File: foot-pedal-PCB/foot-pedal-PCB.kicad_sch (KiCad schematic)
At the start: 14 parts, among them J1 Conn_01x01_Pin, J2 Conn_01x01_Pin, J3 Conn_01x01_Pin, J4 Conn_01x01_Pin, Q1 BT136-600E, SW1 CS12ANW03

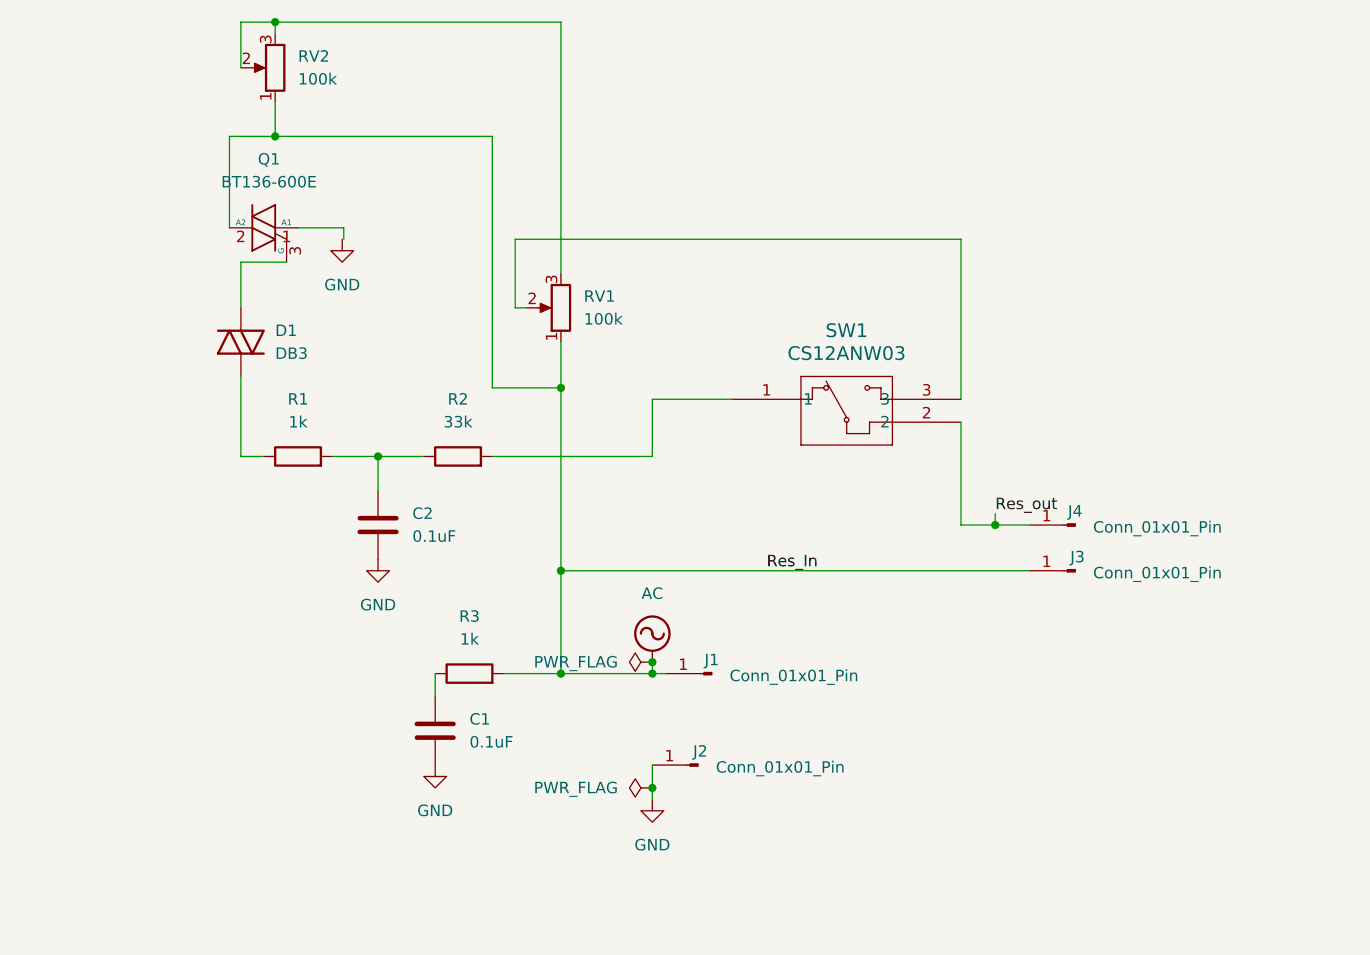
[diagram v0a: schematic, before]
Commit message: fleshed out SPICE, finished pedal schematic v1.0, ordered pedal BOM from mouser.
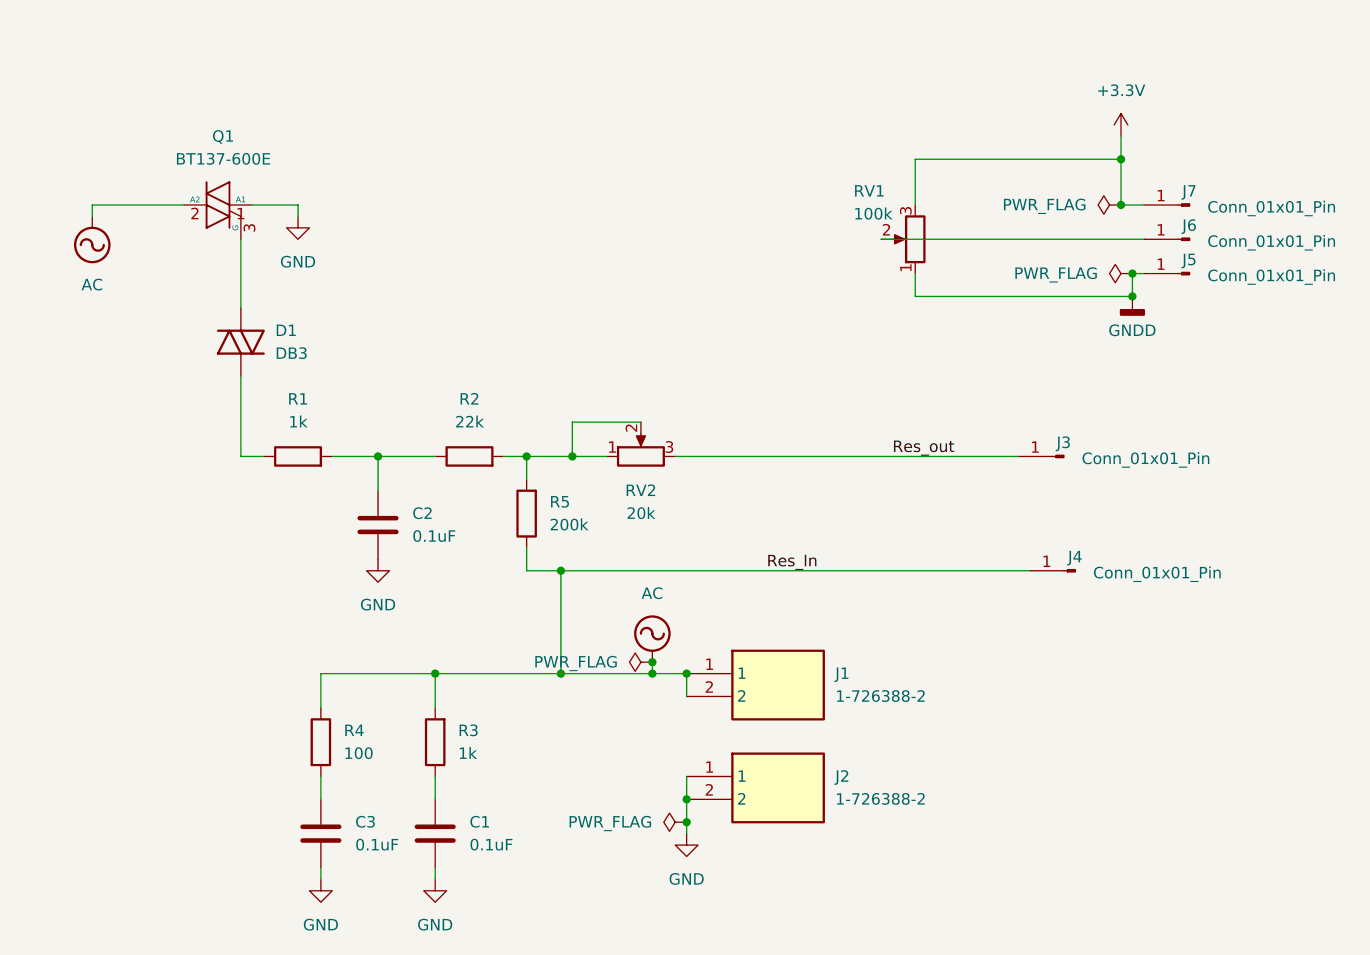
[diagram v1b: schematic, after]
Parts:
- removed J1, J2: Conn_01x01_Pin, symbol Connector:Conn_01x01_Pin
- removed Q1: BT136-600E, Package_TO_SOT_THT:TO-220-3_Vertical, symbol project:BT136-600E
- removed R2: 33k, Resistor_THT:R_Axial_DIN0207_L6.3mm_D2.5mm_P15.24mm_Horizontal, symbol project:R33k
- removed RV2: 100k, Potentiometer_THT:Potentiometer_Vishay_T7-YA_Single_Vertical, symbol project:Trim_pot
- removed SW1: CS12ANW03, footprints:CS12ANW03_NKK, symbol project:CS12ANW03
- added C3: 0.1uF, Capacitor_THT:C_Rect_L18.0mm_W5.0mm_P15.00mm_FKS3_FKP3, symbol project:BFC233627104
- added J1, J2: 1-726388-2, project:17263882, symbol project:1-726388-2
- added J5, J6, J7: Conn_01x01_Pin, Connector_Wire:SolderWire-0.5sqmm_1x01_D0.9mm_OD2.1mm, symbol Connector:Conn_01x01_Pin
- added Q1: BT137-600E, Package_TO_SOT_THT:TO-220-3_Vertical, symbol project:BT137-600E
- added R2: 22k, Resistor_THT:R_Axial_DIN0207_L6.3mm_D2.5mm_P10.16mm_Horizontal, symbol project:R22k
- added R4: 100, Resistor_THT:R_Axial_DIN0516_L15.5mm_D5.0mm_P20.32mm_Horizontal, symbol project:R1003W
- added R5: 200k, Resistor_THT:R_Axial_DIN0207_L6.3mm_D2.5mm_P10.16mm_Horizontal, symbol project:R200k
- added RV2: 20k, project:POT_3329H, symbol project:Trim_pot_20k
- J3, J4: footprint (none) -> Connector_Wire:SolderWire-0.5sqmm_1x01_D0.9mm_OD2.1mm
- R3: footprint Resistor_THT:R_Axial_DIN0207_L6.3mm_D2.5mm_P15.24mm_Horizontal -> Resistor_THT:R_Axial_DIN0207_L6.3mm_D2.5mm_P10.16mm_Horizontal
- RV1: footprint (none) -> project:RA2043F2010EB1B100K
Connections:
- net AC: now also J4.1 (Pin_1), J1.1, J1.2, Q1.2 (A2), R4.1, R5.1; no longer J3.1 (Pin_1), RV1.1
- net GND: now also C3.1, J2.1, J2.2, Q1.1 (A1)
- net Res_out: now also J3.1 (Pin_1), RV2.3; no longer J4.1 (Pin_1)
- net at C2.2, R1.2: now also R2.1
- net at D1.2 (A): now also Q1.3 (G)
- net at RV1.2: now also J6.1 (Pin_1)
- net +3.3V: now reaches RV1.3
- net +3.3V: now also J7.1 (Pin_1)
- new net: R2.2, R5.2, RV2.1, RV2.2
- new net: C3.2, R4.2
- new net GNDD: J5.1 (Pin_1), RV1.1
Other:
- moved on the sheet: C1, R3, RV1

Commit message: Added circuit protection, finished foot pedal PCB design, ordered from OSHPark
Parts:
- added H1: MountingHole, MountingHole:MountingHole_5.5mm, symbol Mechanical:MountingHole
- added J8: Fuse, project:696108003002, symbol project:Fuse Holder
- added RV3: Varistor, project:VAR_B72214P2301K101, symbol project:Varistor
- Q1: footprint Package_TO_SOT_THT:TO-220-3_Vertical -> project:BT137-600E
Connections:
- net AC: now also J8.1, RV3.1; no longer J1.1, J1.2
- net GND: now also RV3.2
- new net: J1.1, J1.2, J8.2
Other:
- moved on the sheet: J1, J2
